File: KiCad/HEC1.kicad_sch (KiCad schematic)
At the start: 2 parts, among them J1 Barrel_Jack_Switch, U12 74LS04

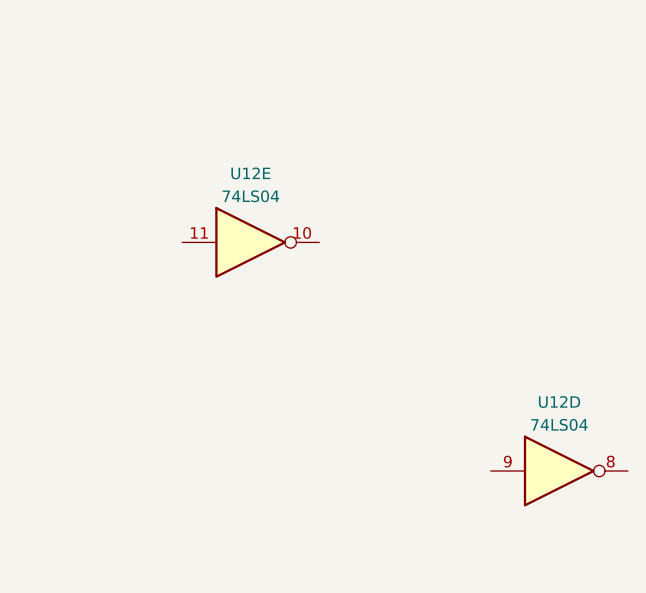
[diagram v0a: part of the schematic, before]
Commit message: Update NMI timing circuit
Updated the NMI generation circuit to prevent a bug occurring when NMI is generated between the rising edge of the last T cycle of an instruction and the falling edge of M1 of the next. Due to delay in M1 signal, the NMI would be qualified one instruction earlier, causing the HEC to enter SYS mode one instruction earlier. If the instruction is an IO instruction by an user program, it can cause a write to any port and potentially destabilize the system.
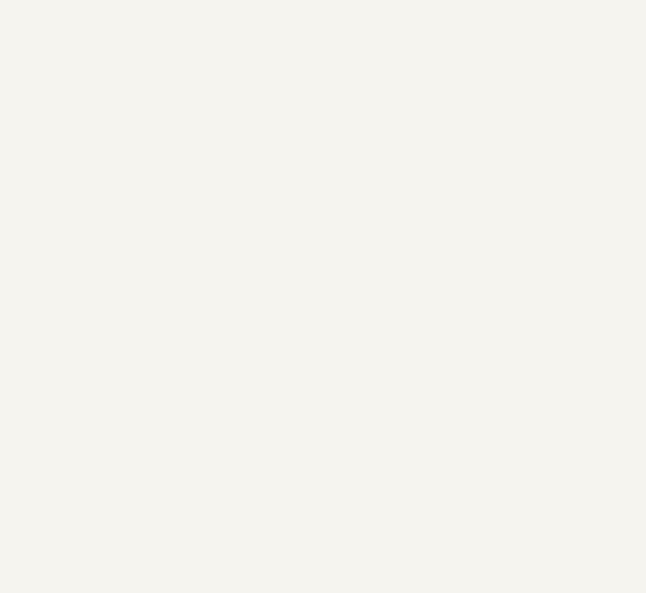
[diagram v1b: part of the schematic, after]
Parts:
- removed U12: 74LS04, Package_DIP:DIP-14_W7.62mm_Socket, symbol 74xx:74LS04
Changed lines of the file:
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@@
-    )
-  )
-  (symbol (lib_id "74xx:74LS04") (at 274.32 127 0) (unit 4)
-    (in_bom yes) (on_board yes) (dnp no) (fields_autoplaced)
-    (property "Reference" "U12" (at 274.32 119.38 0)
-      (effects (font (size 1.27 1.27)))
-    )
-    (property "Value" "74LS04" (at 274.32 121.92 0)
-      (effects (font (size 1.27 1.27)))
-    )
-    (property "Footprint" "Package_DIP:DIP-14_W7.62mm_Socket" (at 274.32 127 0)
-      (effects (font (size 1.27 1.27)) hide)
-    )
-    (property "Datasheet" "http://www.ti.com/lit/gpn/sn74LS04" (at 274.32 127 0)
-      (effects (font (size 1.27 1.27)) hide)
-    )
-    (pin "1")
-    (pin "2")
-    (pin "3")
-    (pin "4")
-    (pin "5")
-    (pin "6")
-    (pin "8")
-    (pin "9")
-    (pin "10")
-    (pin "11")
-    (pin "12")
-    (pin "13")
-    (pin "14")
-    (pin "7")
-    (instances
-      (project "HEC1"
-        (path "/87935374-b60a-4f41-99da-94b76103dd77"
-          (reference "U12") (unit 4)
-        )
-      )
-    )
-  )
-  (symbol (lib_id "74xx:74LS04") (at 240.03 101.6 0) (unit 5)
-    (in_bom yes) (on_board yes) (dnp no) (fields_autoplaced)
-    (property "Reference" "U12" (at 240.03 93.98 0)
-      (effects (font (size 1.27 1.27)))
-    )
-    (property "Value" "74LS04" (at 240.03 96.52 0)
-      (effects (font (size 1.27 1.27)))
-    )
-    (property "Footprint" "Package_DIP:DIP-14_W7.62mm_Socket" (at 240.03 101.6 0)
-      (effects (font (size 1.27 1.27)) hide)
-    )
-    (property "Datasheet" "http://www.ti.com/lit/gpn/sn74LS04" (at 240.03 101.6 0)
-      (effects (font (size 1.27 1.27)) hide)
-    )
-    (pin "1")
-    (pin "2")
-    (pin "3")
-    (pin "4")
-    (pin "5")
-    (pin "6")
-    (pin "8")
-    (pin "9")
-    (pin "10")
-    (pin "11")
-    (pin "12")
-    (pin "13")
-    (pin "14")
-    (pin "7")
-    (instances
-      (project "HEC1"
-        (path "/87935374-b60a-4f41-99da-94b76103dd77"
-          (reference "U12") (unit 5)
-        )
-      )
     )
   )

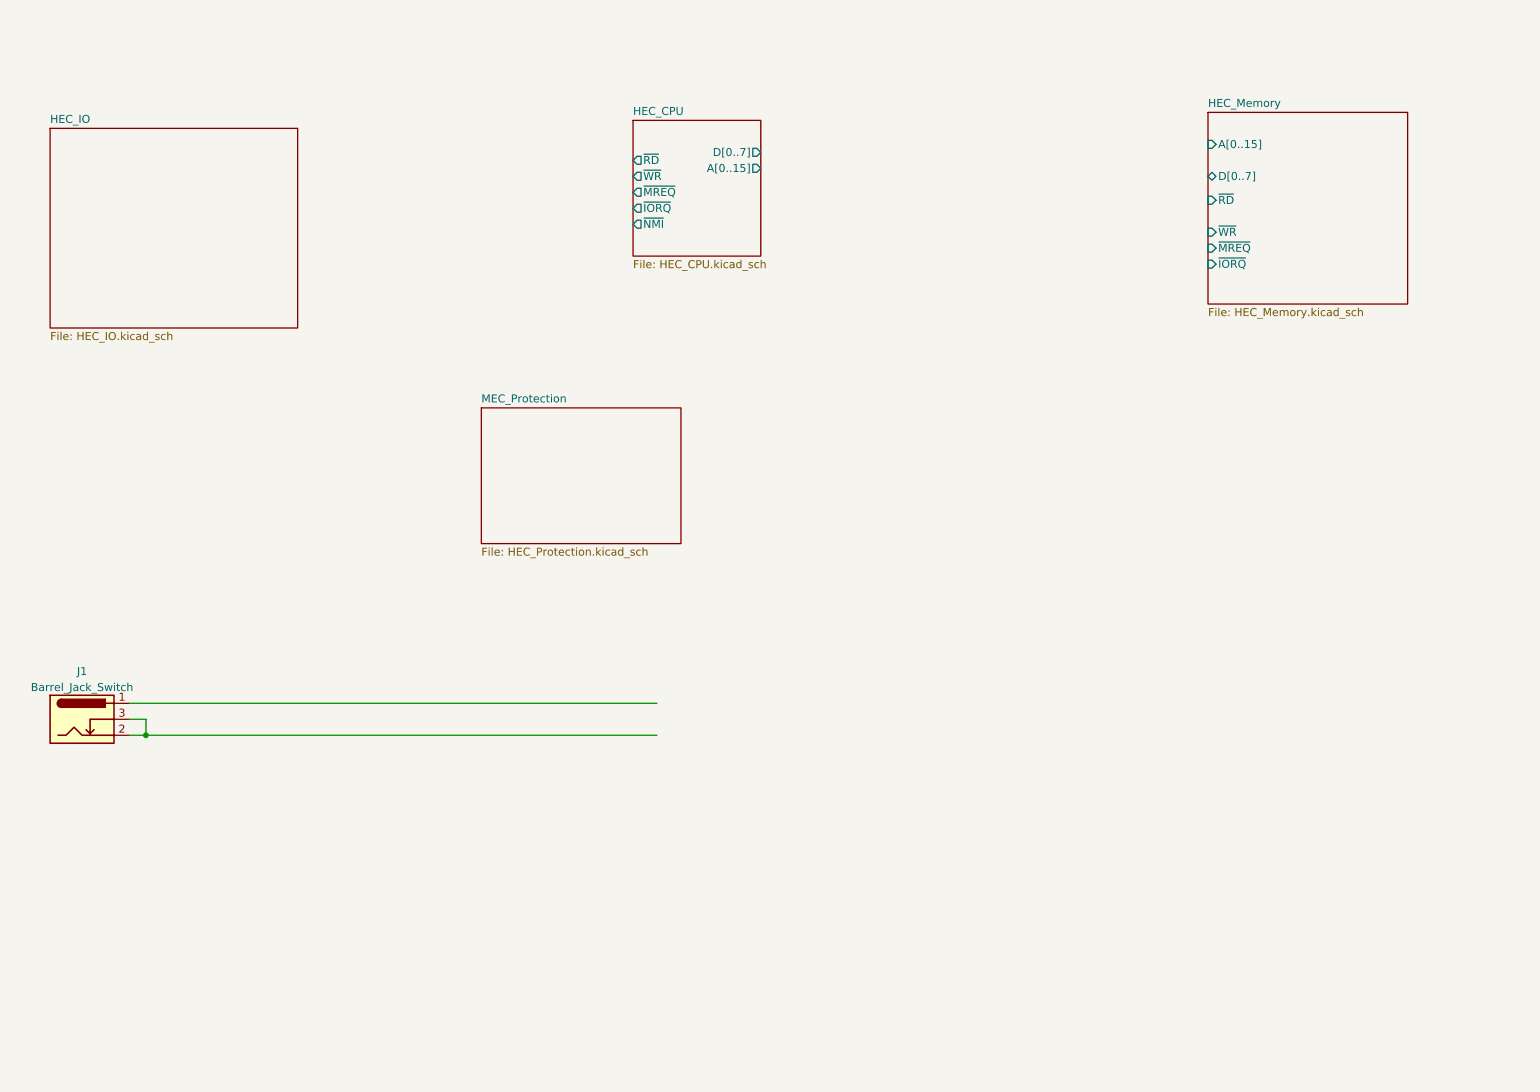
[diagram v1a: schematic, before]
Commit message: Add HEC Bus
The HEC bus packs a lot of information into a small amount of pins. It is suitable for cards with various complexity.
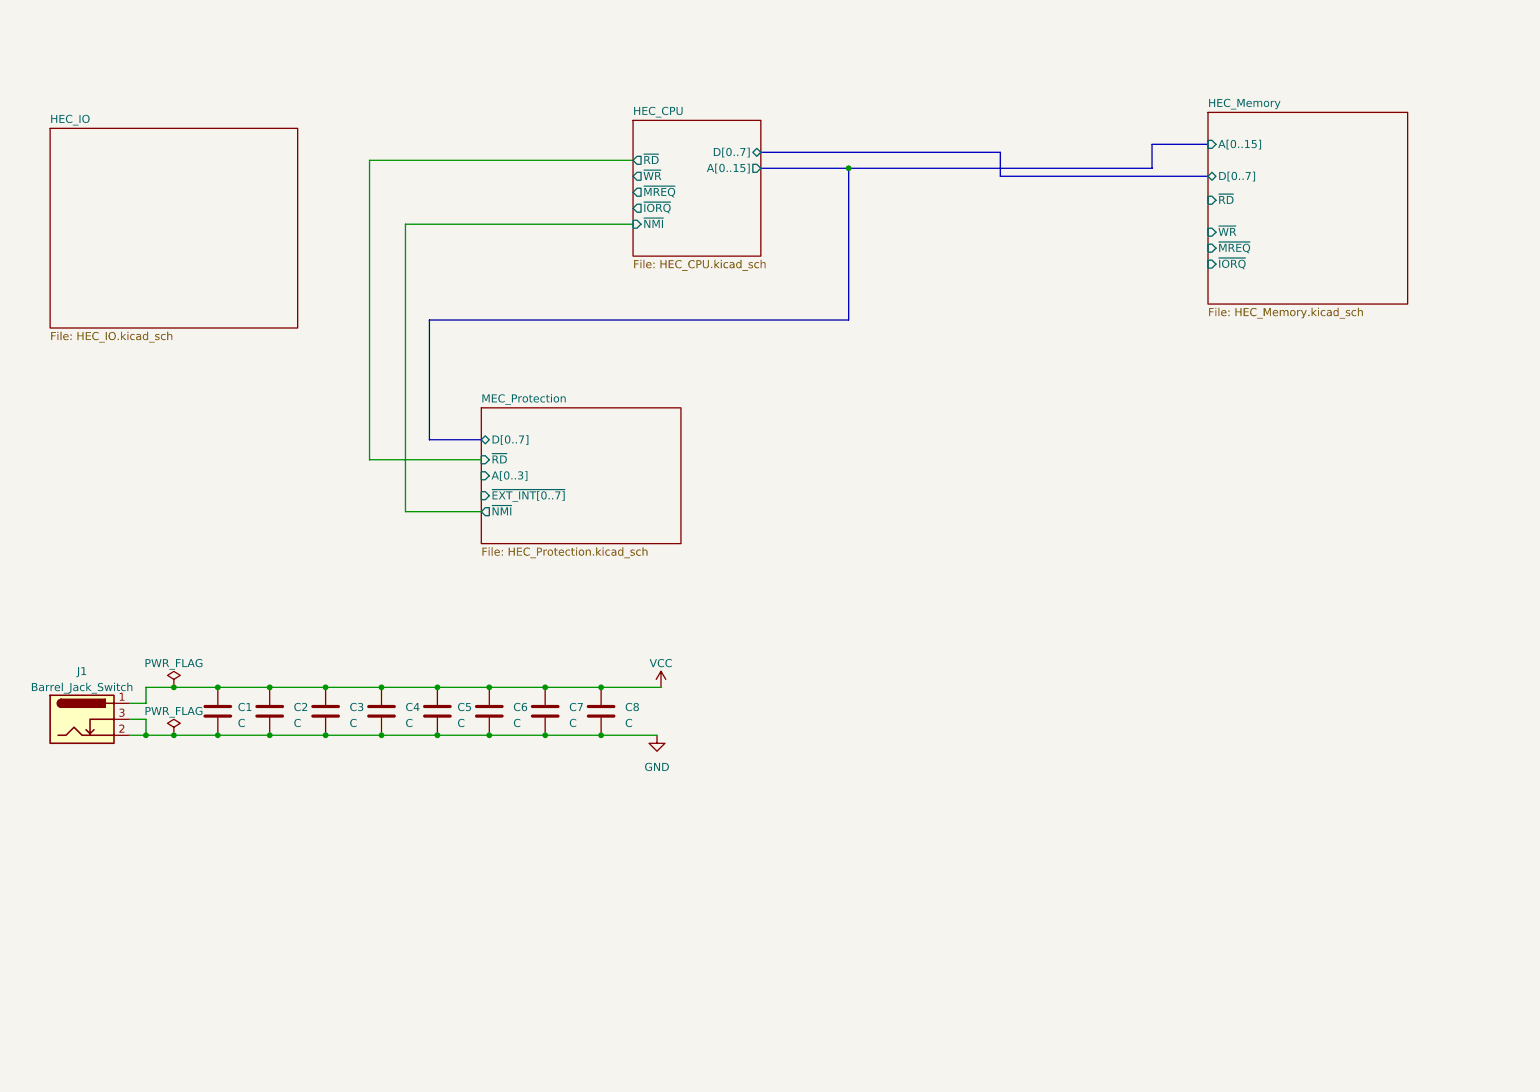
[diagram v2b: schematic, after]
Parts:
- added C1, C2, C3, C4, C5, C6, C7, C8: C, symbol Device:C
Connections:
- net VCC: now reaches J1.1
- net VCC: now also C1.1, C2.1, C3.1, C4.1, C5.1, C6.1, C7.1, C8.1
- net GND: now reaches J1.2, J1.3
- net GND: now also C1.2, C2.2, C3.2, C4.2, C5.2, C6.2, C7.2, C8.2
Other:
- sheet MEC_Protection ports: added A[0..3], D[0..7], ~{EXT_INT[0..7]}, ~{NMI}, ~{RD}; removed none

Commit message: Created footprint for HEC bus
Created footprints for HEC bus and some other updates.
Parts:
- C1, C2, C3, C4, C5, C6, C7, C8: footprint (none) -> Capacitor_THT:C_Disc_D7.0mm_W2.5mm_P5.00mm
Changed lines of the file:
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@@
       (effects (font (size 1.27 1.27)) (justify left))
     )
-    (property "Footprint" "" (at 100.6602 137.16 0)
+    (property "Footprint" "Capacitor_THT:C_Disc_D7.0mm_W2.5mm_P5.00mm" (at 100.6602 137.16 0)
       (effects (font (size 1.27 1.27)) hide)
     )
@@
       (effects (font (size 1.27 1.27)) (justify left))
     )
-    (property "Footprint" "" (at 126.6952 137.16 0)
+    (property "Footprint" "Capacitor_THT:C_Disc_D7.0mm_W2.5mm_P5.00mm" (at 126.6952 137.16 0)
       (effects (font (size 1.27 1.27)) hide)
     )
@@
       (effects (font (size 1.27 1.27)) (justify left))
     )
-    (property "Footprint" "" (at 117.8052 137.16 0)
+    (property "Footprint" "Capacitor_THT:C_Disc_D7.0mm_W2.5mm_P5.00mm" (at 117.8052 137.16 0)
       (effects (font (size 1.27 1.27)) hide)
     )
@@
       (effects (font (size 1.27 1.27)) (justify left))
     )
-    (property "Footprint" "" (at 91.7702 137.16 0)
+    (property "Footprint" "Capacitor_THT:C_Disc_D7.0mm_W2.5mm_P5.00mm" (at 91.7702 137.16 0)
       (effects (font (size 1.27 1.27)) hide)
     )
@@
       (effects (font (size 1.27 1.27)) (justify left))
     )
-    (property "Footprint" "" (at 74.6252 137.16 0)
+    (property "Footprint" "Capacitor_THT:C_Disc_D7.0mm_W2.5mm_P5.00mm" (at 74.6252 137.16 0)
       (effects (font (size 1.27 1.27)) hide)
     )
@@
       (effects (font (size 1.27 1.27)) (justify left))
     )
-    (property "Footprint" "" (at 109.5502 137.16 0)
+    (property "Footprint" "Capacitor_THT:C_Disc_D7.0mm_W2.5mm_P5.00mm" (at 109.5502 137.16 0)
       (effects (font (size 1.27 1.27)) hide)
     )
@@
       (effects (font (size 1.27 1.27)) (justify left))
     )
-    (property "Footprint" "" (at 82.8802 137.16 0)
+    (property "Footprint" "Capacitor_THT:C_Disc_D7.0mm_W2.5mm_P5.00mm" (at 82.8802 137.16 0)
       (effects (font (size 1.27 1.27)) hide)
     )
@@
       (effects (font (size 1.27 1.27)) (justify left))
     )
-    (property "Footprint" "" (at 135.5852 137.16 0)
-      (effects (font (size 1.27 1.27)) hide)
-    )
+    (property "Footprint" "Capacitor_THT:C_Disc_D7.0mm_W2.5mm_P5.00mm" (at 135.5852 137.16 0)
+      (effects (font (size 1.27 1.27)) hide)
+    )

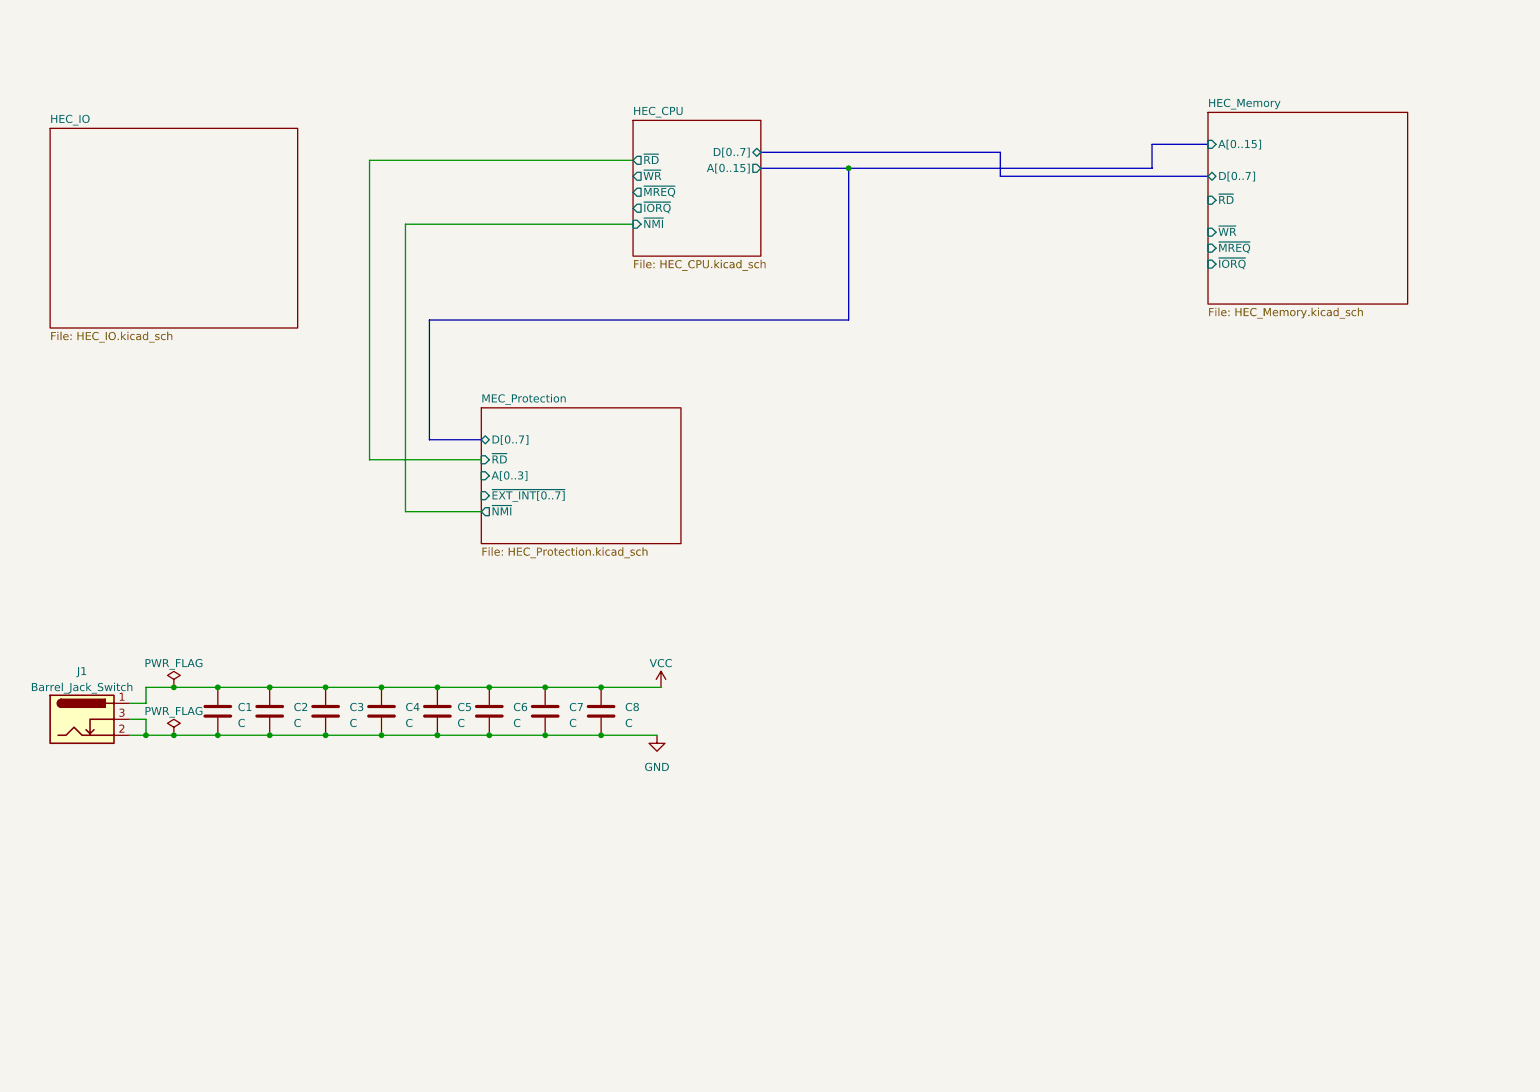
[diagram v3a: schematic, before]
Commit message: IO implementation
Implemented most of IO functions, add connections between the schematics.
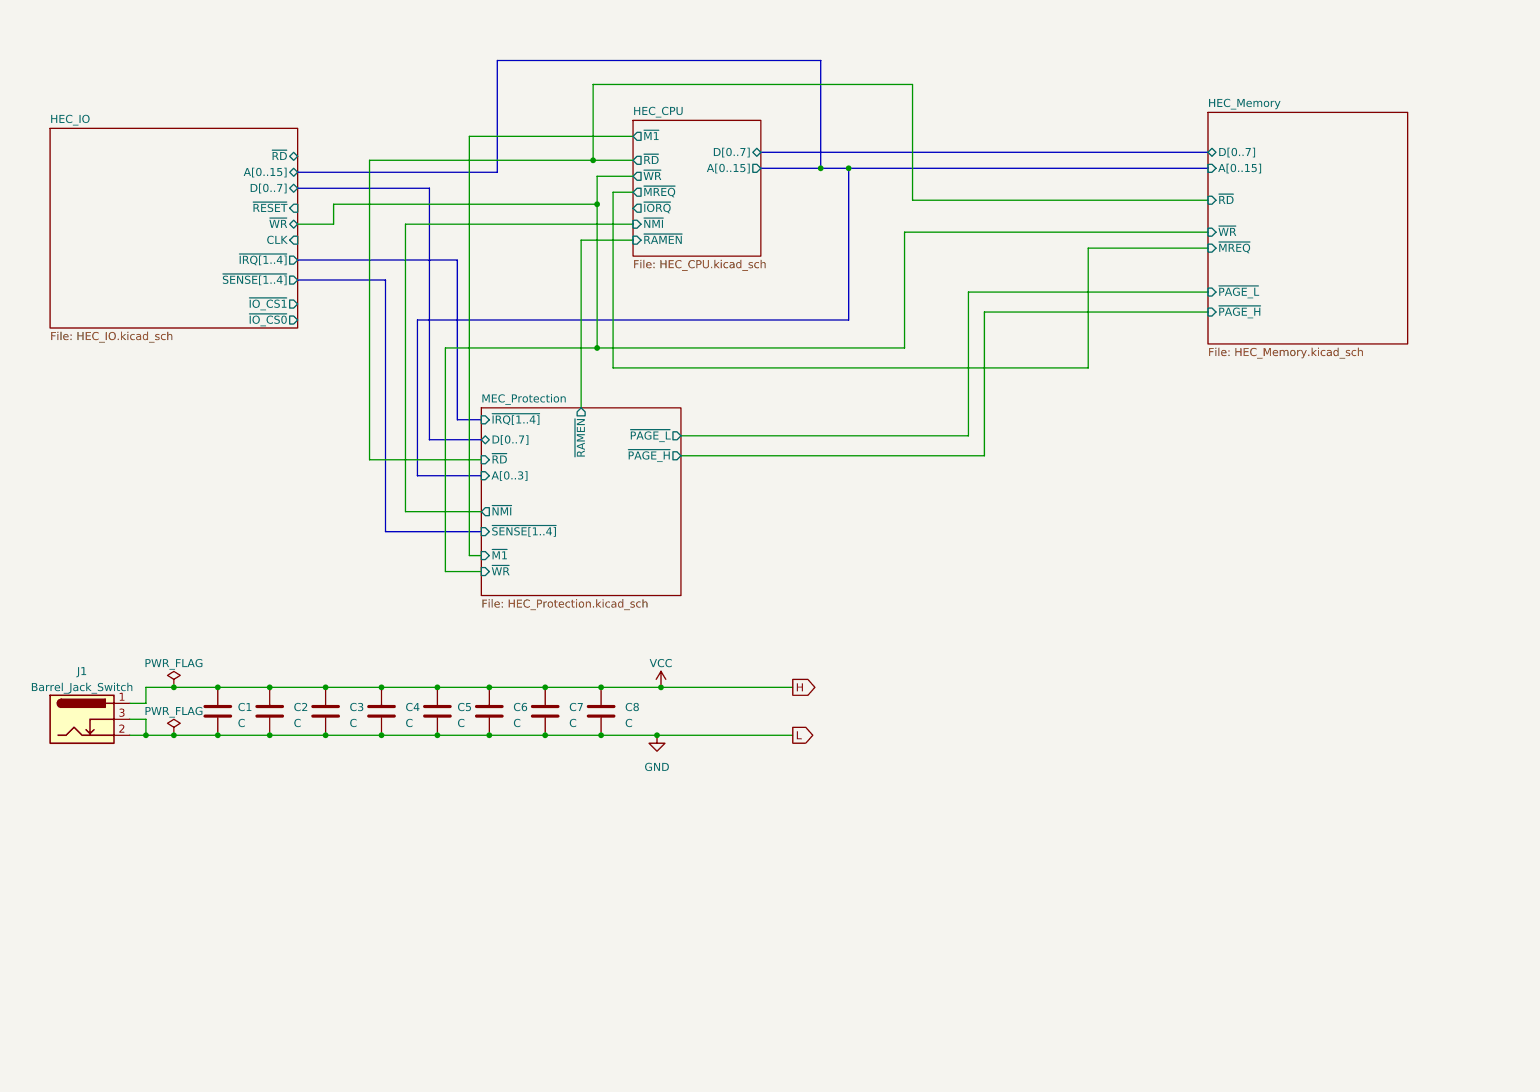
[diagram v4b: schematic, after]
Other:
- sheet HEC_CPU ports: added ~{M1}, ~{RAMEN}; removed none
- sheet HEC_IO ports: added A[0..15], CLK, D[0..7], ~{IO_CS0}, ~{IO_CS1}, ~{IRQ[1..4]}, ~{RD}, ~{RESET}, ~{SENSE[1..4]}, ~{WR}; removed none
- sheet HEC_Memory ports: added ~{PAGE_H}, ~{PAGE_L}; removed ~{IORQ}
- sheet MEC_Protection ports: added ~{IRQ[1..4]}, ~{M1}, ~{PAGE_H}, ~{PAGE_L}, ~{RAMEN}, ~{SENSE[1..4]}, ~{WR}; removed ~{EXT_INT[0..7]}
